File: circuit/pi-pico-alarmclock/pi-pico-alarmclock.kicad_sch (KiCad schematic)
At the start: 38 parts, among them J1 Screw_Terminal_2_P5.00mm, J2 BTN GREEN, J3 BTN BLUE, J4 BTN_YELLOW, J5 NEOPIXEL, J6 OLED, J7 BAT - Screw_Terminal_2_P5.00mm, Q1 IRLZ44N, Q2 IRLZ44N, Q3 IRF9540, Q4 IRLZ44N, U1 Pico, U3 TC4056A Charger Module

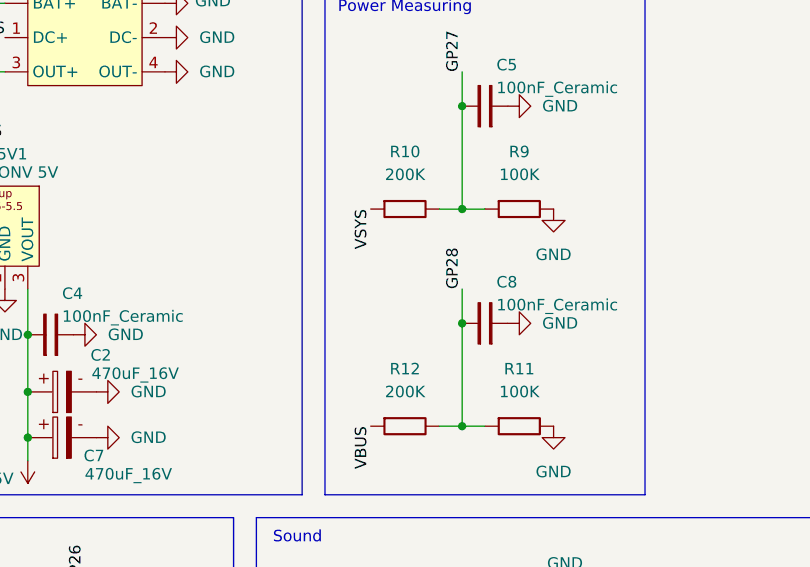
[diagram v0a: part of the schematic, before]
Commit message: Update resistors to 220K and bump revision
Set several 200K resistor values to 220K in schematic and PCB. Bump
project version/revision to v0.4 (01.2026 / 2026-01-06). Regenerate PCB
footprint UUIDs.
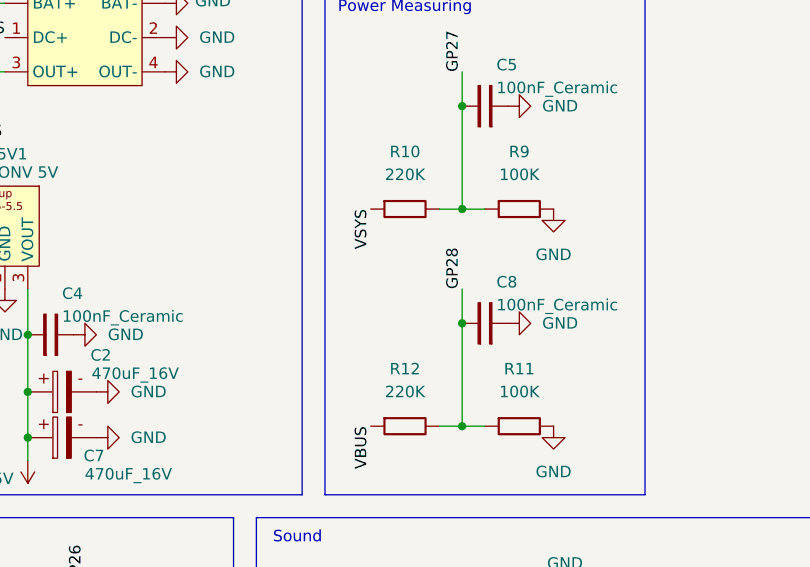
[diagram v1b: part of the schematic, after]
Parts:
- R10, R12: value 200K -> 220K
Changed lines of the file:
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@@
 	(title_block
 		(title "pi-pico-alarmclock-rust")
-		(date "2025-11-20")
-		(rev "v0.3")
+		(date "2026-01-06")
+		(rev "v0.4")
 		(company "rafael")
 	)
@@
 			)
 		)
-		(property "Value" "200K"
+		(property "Value" "220K"
 			(at 195.58 97.79 0)
 			(effects
@@
 			)
 		)
-		(property "Value" "200K"
+		(property "Value" "220K"
 			(at 195.58 73.66 0)
 			(effects
